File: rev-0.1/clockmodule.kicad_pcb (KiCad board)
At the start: 2 copper layers, 90 x 65 mm, 41 parts, among them J1 Vin, J2 Clock output, J3 DC Input, SW1 SW_Push, SW2 SW_Push, U1 NE555P, U3 L7805_J, U6 NE555P, U7 NE555P, U8 7400

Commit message: moved to rev-.1 folder
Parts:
- moved RV1 1.00 mm to (109.0, 69.0)
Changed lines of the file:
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@@
-(kicad_pcb (version 20220308) (generator pcbnew)
+(kicad_pcb (version 20220331) (generator pcbnew)
   (general
     (thickness 1.6)
@@
     (pcbplotparams
       (layerselection 0x00010ec_ffffffff)
+      (plot_on_all_layers_selection 0x0000000_00000000)
       (disableapertmacros false)
       (usegerberextensions true)
@@
       (dashed_line_gap_ratio 3.000000)
       (svgprecision 6)
-      (excludeedgelayer true)
       (plotframeref false)
       (viasonmask false)
@@
   )
   (footprint "w_pth_resistors:trimmer_alps-rk09k1130ah1" (layer "F.Cu")
-    (at 109 68)
+    (at 109 69)
     (descr "9mm trimmer, Alps RK09K1130AH1")
     (tags "trimmer")

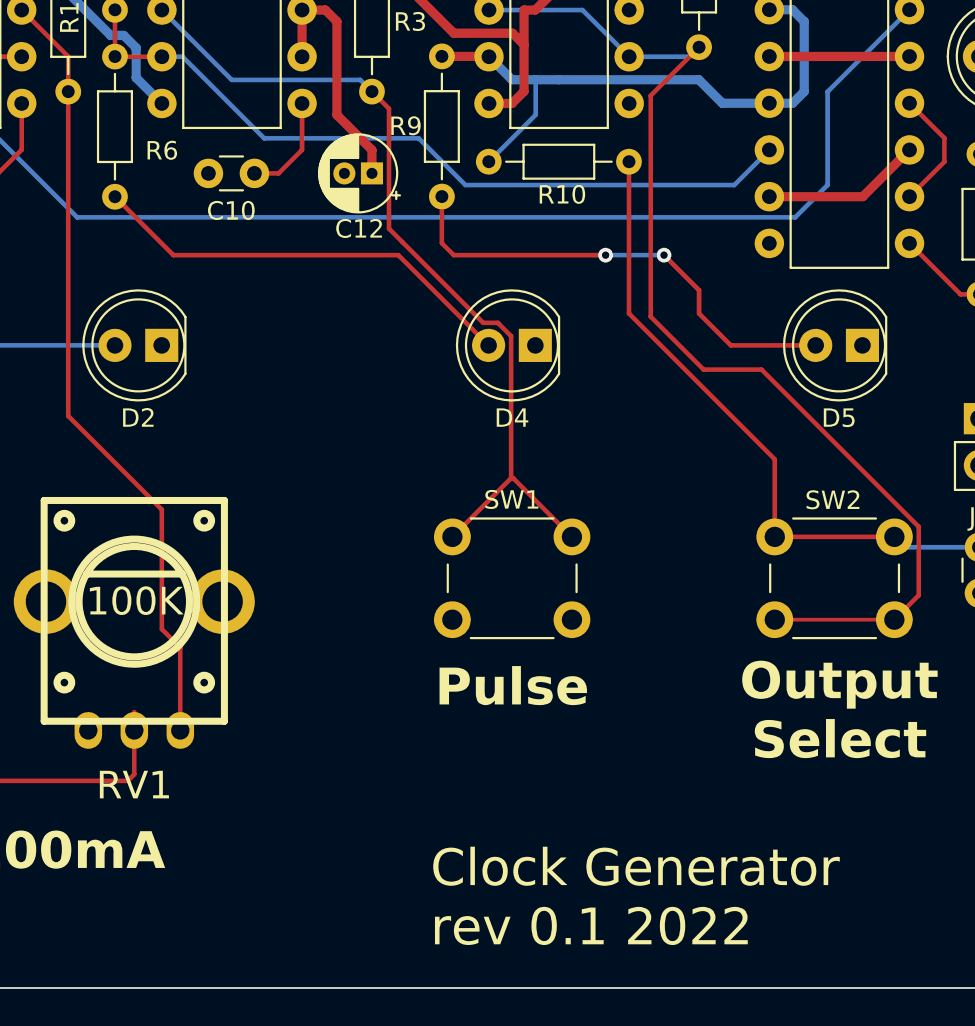
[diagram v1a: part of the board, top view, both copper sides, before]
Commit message: Swapped C4 and C3 silkscreen text
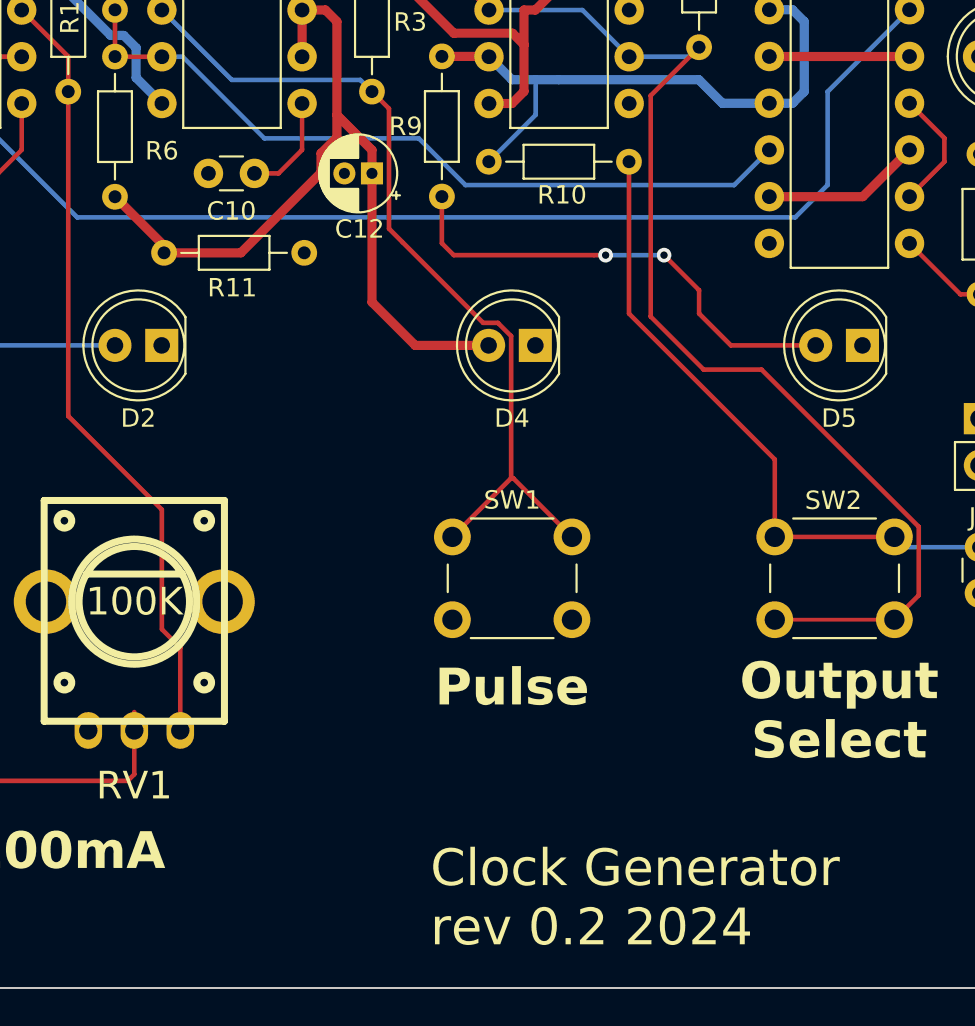
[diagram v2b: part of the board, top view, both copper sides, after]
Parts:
- added R11: 1K, Resistor_THT:R_Axial_DIN0204_L3.6mm_D1.6mm_P7.62mm_Horizontal, F.Cu at (110.6, 50.0)
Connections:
- C12 pad 1: Net-(U6-DIS) -> Net-(D4-A)
- U6 pad 6: Net-(U6-DIS) -> Net-(D4-A)
- U6 pad 7: Net-(U6-DIS) -> Net-(D4-A)
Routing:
- net Net-(D4-A): track 23.7 -> 46.0 mm
- net Net-(U6-DIS): track 13.7 -> 0.00 mm
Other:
- board text added: "Clock Generator rev 0.2 2024"
- board text removed: "Clock Generator rev 0.1 2022"

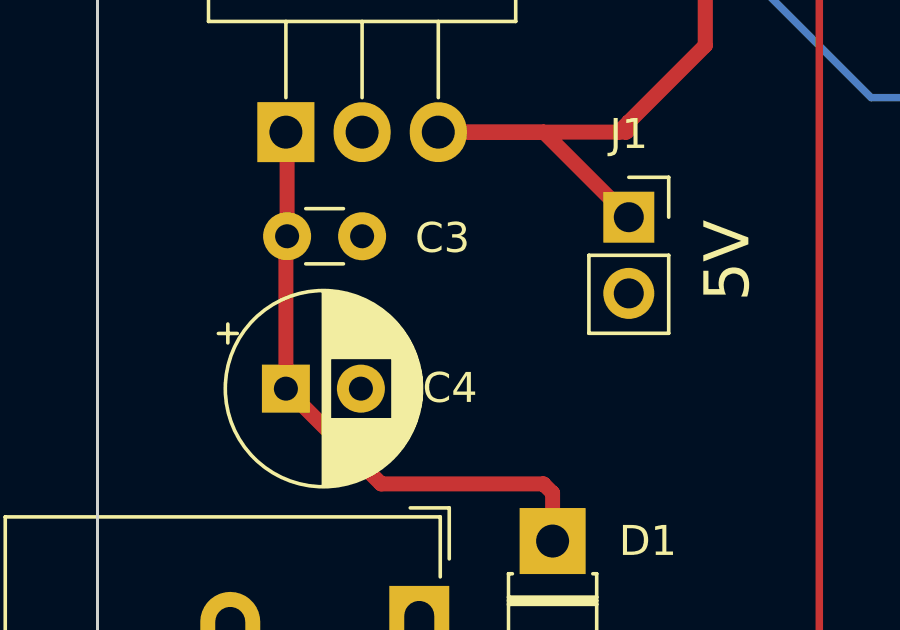
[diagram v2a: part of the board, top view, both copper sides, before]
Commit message: Moved `R11`
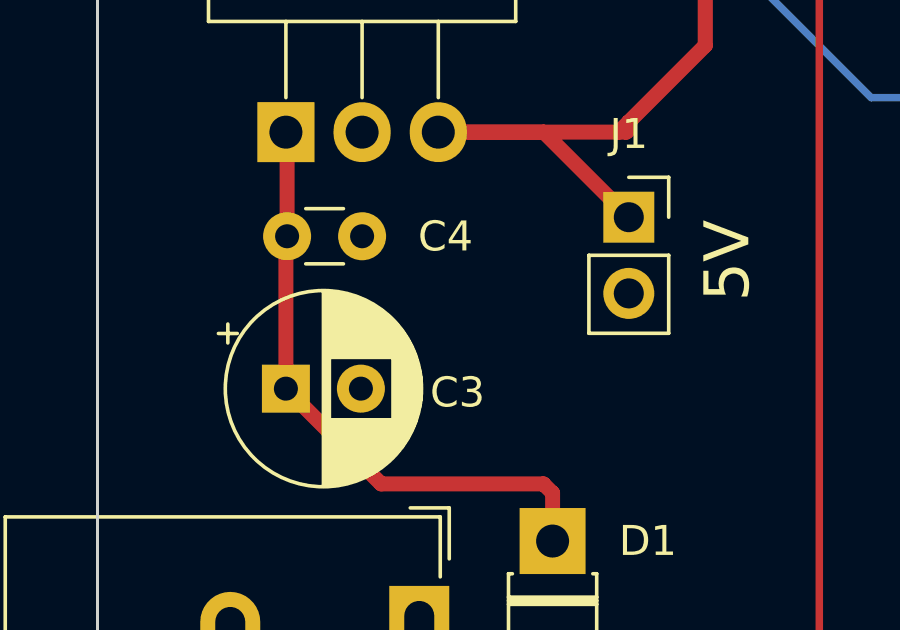
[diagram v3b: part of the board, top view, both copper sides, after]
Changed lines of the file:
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@@
 		(tags "CP Radial series Radial pin pitch 2.50mm  diameter 6.3mm Electrolytic Capacitor")
 		(property "Reference" "C3"
-			(at 5.22 -5.02 0)
+			(at 5.72 0.13 0)
 			(layer "F.SilkS")
 			(effects
@@
 		(tags "C Disc series Radial pin pitch 2.50mm  diameter 3.0mm width 1.6mm Capacitor")
 		(property "Reference" "C4"
-			(at -2.93 -5.06 0)
+			(at -2.78 -0.01 0)
 			(layer "F.SilkS")
 			(effects

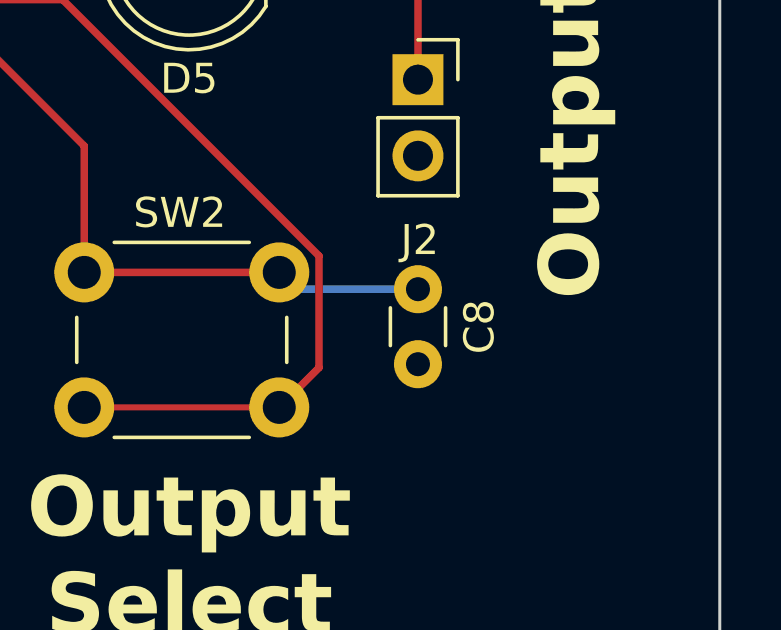
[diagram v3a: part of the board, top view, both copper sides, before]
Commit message: Change `C8` footprint
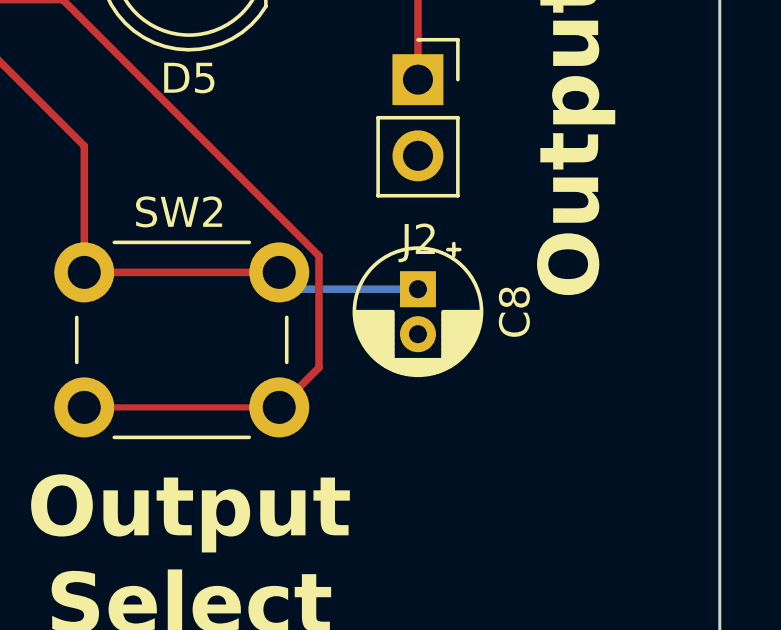
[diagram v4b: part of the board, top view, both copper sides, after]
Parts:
- C8: footprint Capacitor_THT:C_Disc_D3.0mm_W1.6mm_P2.50mm -> Capacitor_THT:CP_Radial_D4.0mm_P1.50mm
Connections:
- C12 pad 1: Net-(D4-A) -> Net-(U6-DIS)
- R11 pad 1: Net-(D4-A) -> Net-(U6-DIS)
- U6 pad 6: Net-(D4-A) -> Net-(U6-DIS)
- U6 pad 7: Net-(D4-A) -> Net-(U6-DIS)
